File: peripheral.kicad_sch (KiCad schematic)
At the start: 6 parts, among them U40 8255A

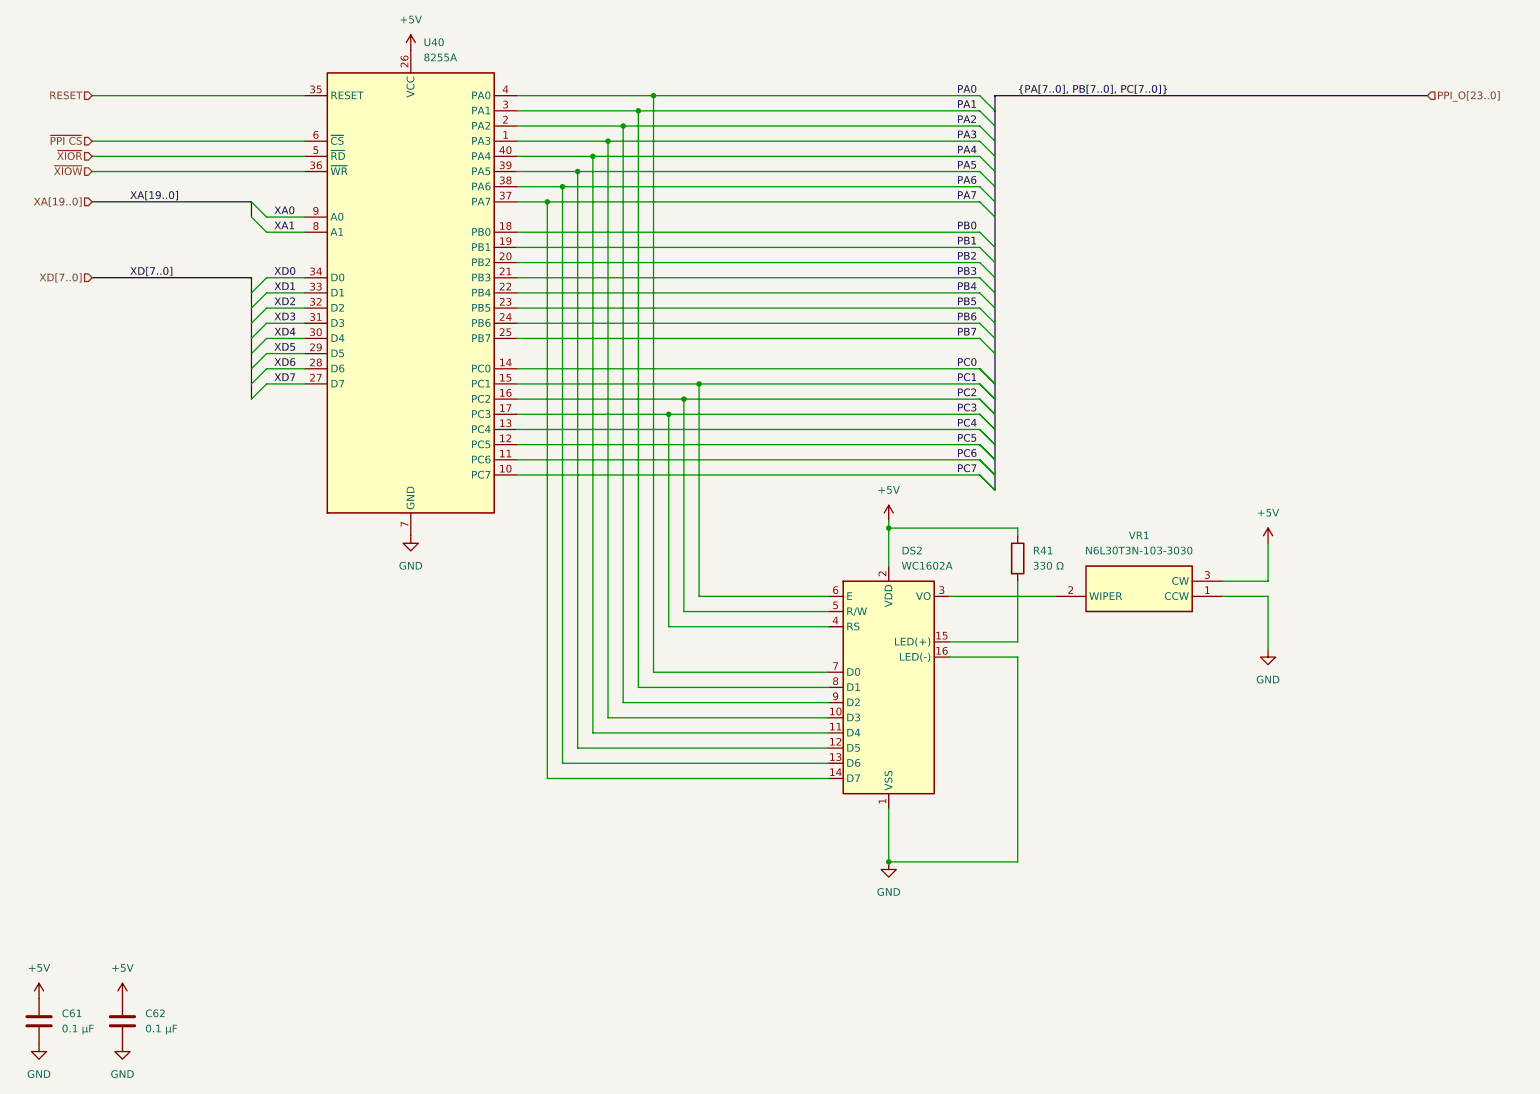
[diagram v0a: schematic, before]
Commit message: Upgraded speaker, esd protection, added dip sockets, adjusted routing
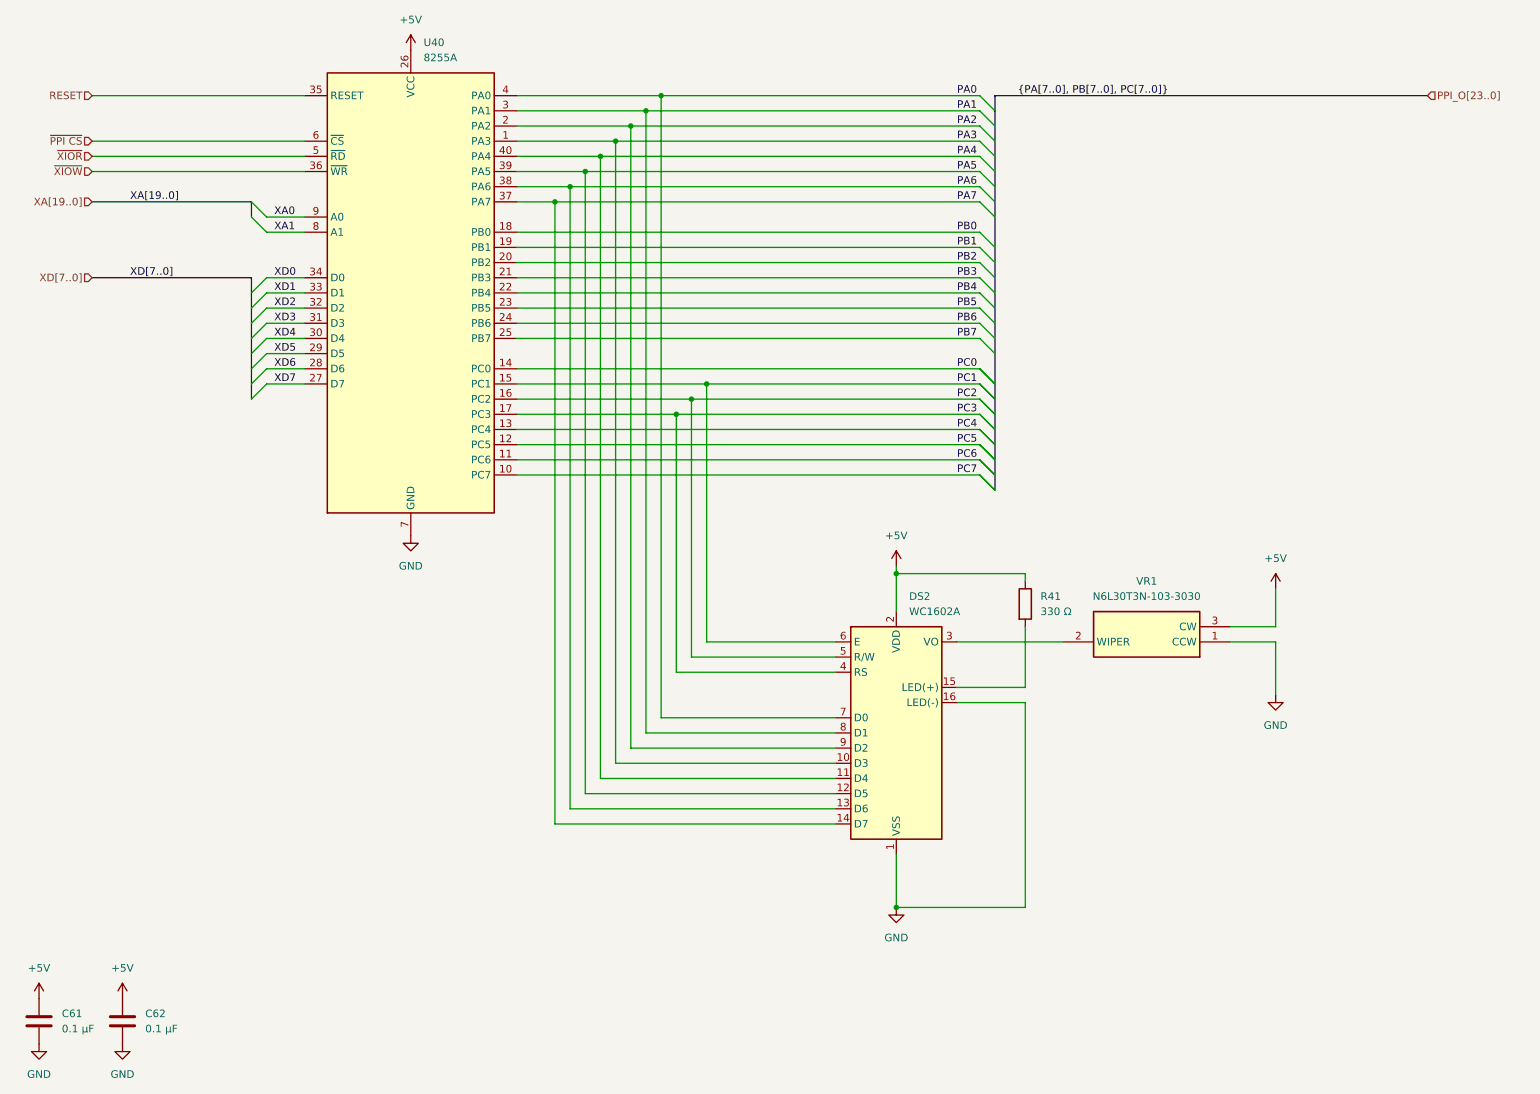
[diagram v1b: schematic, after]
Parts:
- U40: footprint Package_DIP:DIP-40_W15.24mm -> Package_DIP:DIP-40_W15.24mm_Socket
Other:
- moved on the sheet: DS2, R41, VR1

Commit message: final commit before spinning
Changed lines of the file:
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@@
 		)
 	)
-	(label "XA[19..0]"
+	(label "XA[9..0]"
 		(at 34.29 48.26 0)
 		(effects
@@
 		)
 	)
-	(hierarchical_label "XA[19..0]"
+	(hierarchical_label "XA[9..0]"
 		(shape input)
 		(at 27.94 48.26 180)
@@
 		)
 	)
-	(hierarchical_label "PPI_O[23..0]"
-		(shape input)
+	(hierarchical_label "PPI_O"
+		(shape bidirectional)
 		(at 251.46 30.48 0)
 		(effects
